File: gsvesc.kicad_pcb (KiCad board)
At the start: 4 copper layers, 111 x 111 mm, 147 parts, among them J1 Conn_01x06, J10 PHASE_C, J11 PHASE_B, J12 NTC, J13 Conn_01x02, J14 Conn_01x03, J2 Conn_01x06, J3 Conn_01x06, J4 Conn_01x05, J5 Conn_01x03, J6 USB_B_Mini, J7 BAT+, J8 BAT-, J9 PHASE_A, Q1 TPH2R608NH,L1Q, Q2 TPH2R608NH,L1Q, Q3 TPH2R608NH,L1Q, Q4 TPH2R608NH,L1Q, Q5 TPH2R608NH,L1Q, Q6 TPH2R608NH,L1Q, U1 STM32F405RGTx, U10 LM5008MM, U11 SN74LVC1G66DBVR, U12 LM5107, U13 SN74LVC1G66DBVR, U14 TPS5430DDA, U15 LM5107, U16 EYSGJNZWY, U17 TMP100NA_250, U2 SN74LVC1G66DBVR, U3 LM5107, U4 INA240A2, U5 INA240A2, U6 INA240A2, U7 SN74LVC1G66DBVR, U8 SN74LVC1G66DBVR, U9 SN74LVC1G66DBVR, Y1 X50328MSB2GI

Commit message: Ready for JLC
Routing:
- net /MCU/CURRENT_2: track 52.3 -> 48.8 mm
- net /Driver/SENS_FILTER: track 35.4 -> 36.2 mm
- net /MCU/I2C1_SCL: track 70.7 -> 70.1 mm

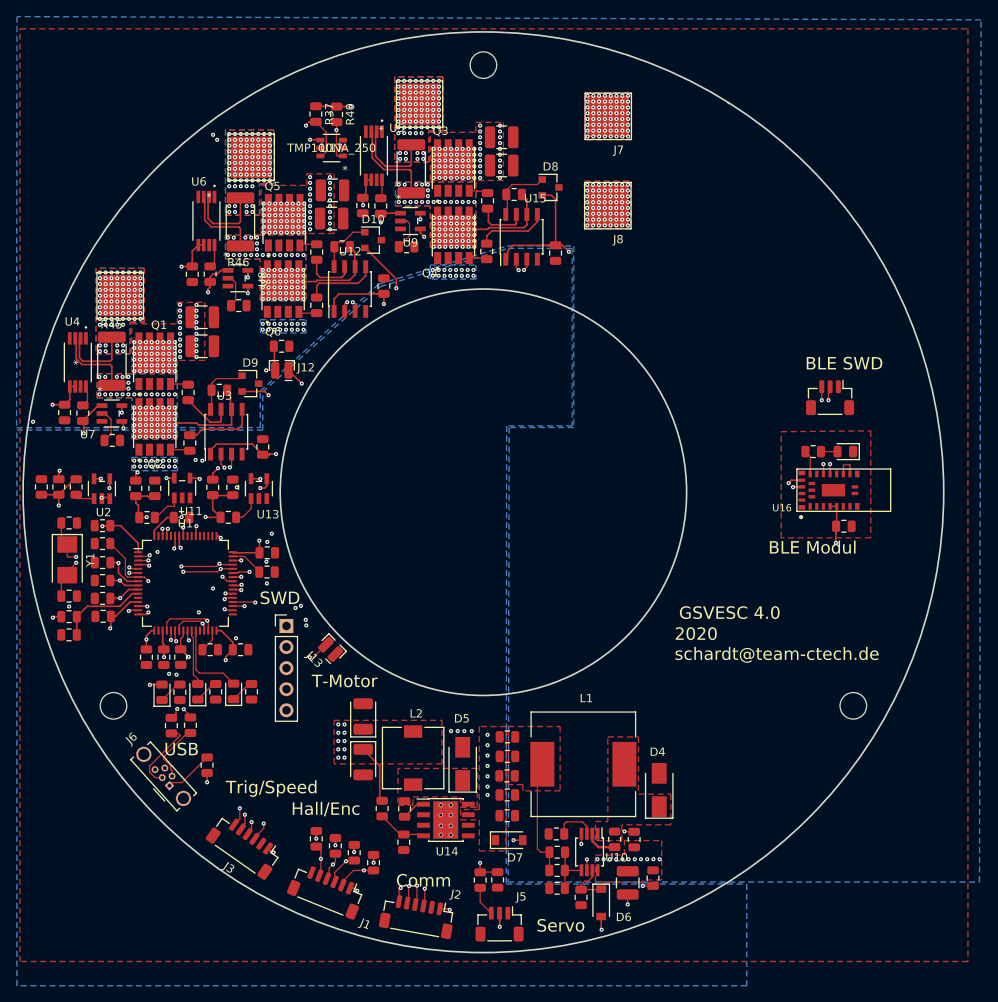
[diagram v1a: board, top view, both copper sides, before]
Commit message: some bug fixes for next pcb-run
- Add JST connector for Motor Temp
- Remove USB 5V
- add correct footprint for D8,9,10
- add JST connector for external off
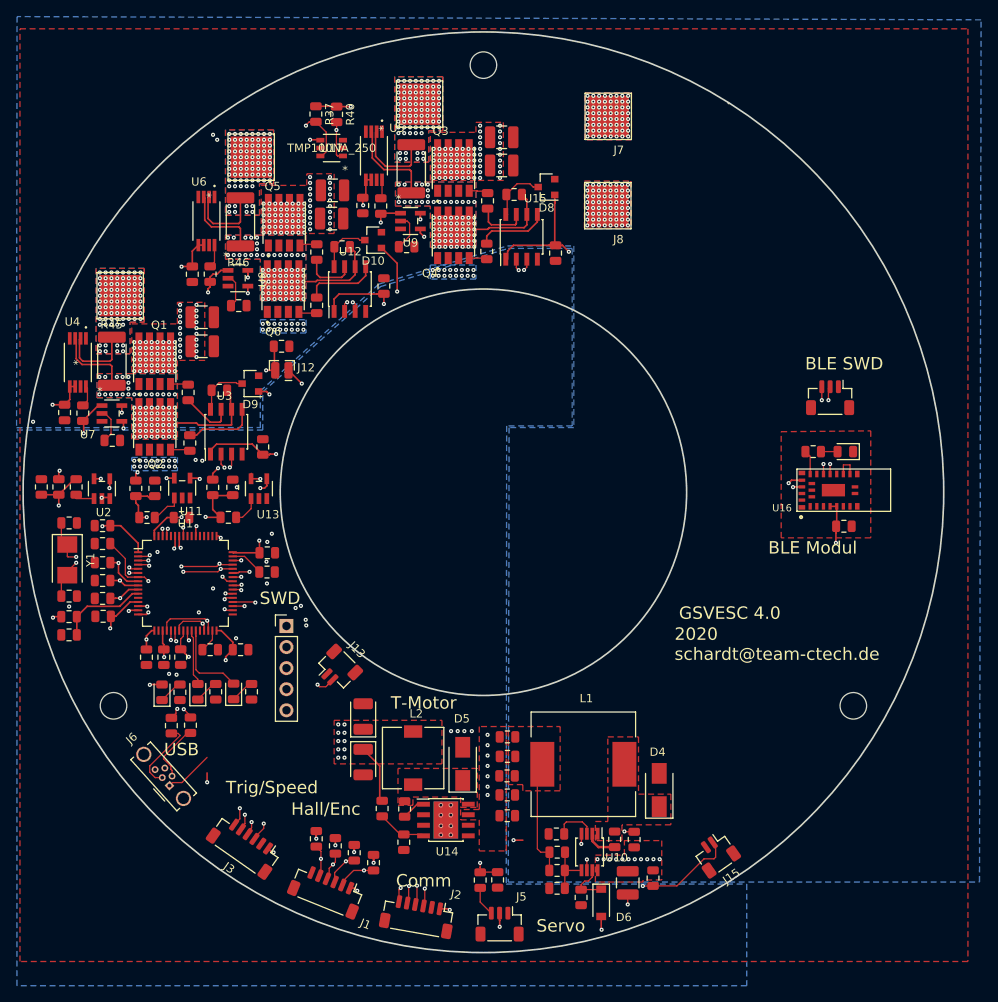
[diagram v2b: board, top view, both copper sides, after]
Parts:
- removed D7: B5819W, Diode_SMD:D_SOD-123
- removed R1: 0R00, Resistor_SMD:R_0805_2012Metric
- added J15: EXT off, Connector_JST:JST_SH_BM02B-SRSS-TB_1x02-1MP_P1.00mm_Vertical, F.Cu at (128.0, 143.6)
- J13: value Conn_01x02 -> T-Motor; footprint gsvesc:2pad_smd_testpin -> Connector_JST:JST_SH_BM02B-SRSS-TB_1x02-1MP_P1.00mm_Vertical
- R37, R40: value R -> 10k0
- moved J13 2.27 mm to (82.4, 121.3), turned to 315 degrees
- moved D8 0.50 mm to (107.6, 63.2), turned to 180 degrees
- turned D10 to 180 degrees
- turned D9 to 180 degrees
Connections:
- D10 pad 1: Net-(C27-Pad1) -> +12V
- D10 pad 2: +12V -> (no net)
- D10 pad 3: (no net) -> Net-(C27-Pad1)
- D8 pad 1: Net-(C32-Pad1) -> +12V
- D8 pad 2: +12V -> (no net)
- D8 pad 3: (no net) -> Net-(C32-Pad1)
- D9 pad 1: Net-(C21-Pad1) -> +12V
- D9 pad 2: +12V -> (no net)
- D9 pad 3: (no net) -> Net-(C21-Pad1)
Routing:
- net /Driver/EXT_OFF: track 10.6 -> 21.5 mm
- net +12V: track 46.9 -> 43.5 mm
- net /MCU/TEMP_MOTOR: track 54.3 -> 52.4 mm
- net Net-(C21-Pad1): track 7.24 -> 6.46 mm

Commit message: BUG Fixes, see BUGS.txt
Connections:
- net Net-(U1-Pad53) renamed /MCU/PC12
- U1 pad 51: Net-(U1-Pad51) -> /NRF/NRF_TX
- U1 pad 52: Net-(U1-Pad52) -> /NRF/NRF_RX
- U1 pad 57: /MCU/SERVO -> /MCU/PB5
- U1 pad 58: /NRF/NRF_TX -> /MCU/PB6
- U1 pad 59: /NRF/NRF_RX -> /MCU/SERVO
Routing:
- net +5V: track 42.1 -> 0.00 mm, vias 2 -> 0
- net Net-(J6-Pad1): track 5.94 -> 0.00 mm
- net /NRF/NRF_TX: track 111.3 -> 108.5 mm
- net /NRF/NRF_RX: track 111.6 -> 109.3 mm
- net /MCU/SERVO: track 65.4 -> 66.2 mm

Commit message: bug fixing
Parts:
- added U18: AQY282S, Package_SO:SO-4_4.4x4.3mm_P2.54mm, F.Cu at (126.2, 143.0)
- J15: value EXT off -> EXT_OFF; footprint Connector_JST:JST_SH_BM02B-SRSS-TB_1x02-1MP_P1.00mm_Vertical -> Connector_JST:JST_SH_BM06B-SRSS-TB_1x06-1MP_P1.00mm_Vertical
- moved J15 10.4 mm to (136.0, 137.0), turned to 221 degrees
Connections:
- J15 pad 1: /Driver/EXT_OFF -> VBAT
- J15 pad 2: GND -> +12V
- R12 pad 1: /Driver/EXT_OFF -> /Driver/EXT_OFF_DIRECT
- U10 pad 6: /Driver/EXT_OFF -> /Driver/EXT_OFF_DIRECT
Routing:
- net /Driver/EXT_OFF_DIRECT: track 0.00 -> 31.2 mm, vias 0 -> 2
- net +12V: track 43.5 -> 61.9 mm, vias 13 -> 14
- net /Driver/EXT_OFF: track 21.5 -> 10.7 mm, vias 2 -> 0
- net VCC: track 78.9 -> 81.0 mm, vias 38 -> 39
- net VBAT: track 25.7 -> 27.6 mm, vias 281 -> 282
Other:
- board text added: "4: drive max 2mA 5: pull to GND"
- board text added: "EXT off"
- board text added: "GND"
- board text added: "Ph A"
- board text added: "Ph B"
- board text added: "Ph C"
- board text added: "VBAT"

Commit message: add PDF
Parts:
- moved C24 0.45 mm to (70.9, 77.4), turned to 180 degrees
- moved C46 0.35 mm to (85.8, 65.4)
- moved R33 0.29 mm to (87.9, 65.4)
- moved U18 0.20 mm to (126.2, 142.8)
- moved C44 0.10 mm to (81.7, 63.6)
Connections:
- net /Driver/EXT_OFF renamed /Driver/EN_3V3
- J15 pad 5: /Driver/EXT_OFF_DIRECT -> /Driver/EN_12V
- R12 pad 1: /Driver/EXT_OFF_DIRECT -> /Driver/EN_12V
- U10 pad 6: /Driver/EXT_OFF_DIRECT -> /Driver/EN_12V
- U18 pad 4: /Driver/EXT_OFF_DIRECT -> Net-(U14-Pad5)
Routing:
- net /Driver/EXT_OFF_DIRECT: track 31.2 -> 0.00 mm, vias 2 -> 0
- net /Driver/EN_12V: track 0.00 -> 30.6 mm, vias 0 -> 3
- net Net-(U14-Pad5): track 0.00 -> 27.5 mm, vias 0 -> 2
- net Net-(C24-Pad1): track 4.13 -> 4.91 mm
- net GND: vias 120 -> 173
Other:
- board text removed: "4: drive max 2mA 5: pull to GND"

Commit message: temp
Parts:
- added C50: 10u0/75V, Capacitor_SMD:C_1210_3225Metric, F.Cu at (76.6, 63.0)
- added C51: 10u0/75V, Capacitor_SMD:C_1210_3225Metric, F.Cu at (117.5, 63.1)
- added C52: 10u0/75V, Capacitor_SMD:C_1210_3225Metric, F.Cu at (97.0, 63.1)
- added C53: CP, Capacitor_SMD:CP_Elec_10x12.5, F.Cu at (142.6, 79.7)
- added C54: CP, Capacitor_SMD:CP_Elec_10x12.5, F.Cu at (131.0, 79.5)
- added C55: CP, Capacitor_SMD:CP_Elec_10x12.5, F.Cu at (135.7, 92.6)
- added C56: CP, Capacitor_SMD:CP_Elec_10x12.5, F.Cu at (147.3, 92.5)
- J14: footprint Connector_JST:JST_SH_BM03B-SRSS-TB_1x03-1MP_P1.00mm_Vertical -> Connector_PinHeader_2.54mm:PinHeader_1x03_P2.54mm_Vertical
- moved J7 59.7 mm to (146.1, 105.7)
- moved J8 45.3 mm to (135.7, 105.7), turned to 270 degrees
- moved C29 38.8 mm to (70.6, 78.7), turned to 90 degrees
- moved R40 37.2 mm to (96.7, 88.7), turned to 180 degrees
- moved R35 37.1 mm to (125.1, 129.2), turned to 180 degrees
- moved U5 37.1 mm to (70.9, 92.9), turned to 180 degrees
- moved D8 37.0 mm to (74.0, 78.8), turned to 90 degrees
- moved R28 36.9 mm to (76.5, 53.1), turned to 180 degrees
- moved R37 36.2 mm to (96.6, 86.5), turned to 180 degrees
- moved D11 36.2 mm to (125.0, 126.2)
- moved J10 34.9 mm to (125.7, 63.3)
- moved U15 34.4 mm to (73.4, 83.8), turned to 0 degrees
- moved C46 34.3 mm to (70.5, 96.1), turned to 0 degrees
- moved R31 33.8 mm to (124.1, 69.2), turned to 180 degrees
- moved J11 33.7 mm to (105.5, 63.4)
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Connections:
- U17 pad 3: Net-(U17-Pad3) -> GND
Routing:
- net /Driver/SH_C: track 64.9 -> 1.64 mm, vias 70 -> 20
- net /MCU/I2C1_SDA: track 69.3 -> 6.15 mm, vias 3 -> 1
- net /POWER/CURR_FILTER: track 71.5 -> 15.7 mm, vias 5 -> 1
- net /MCU/I2C1_SCL: track 70.1 -> 18.2 mm, vias 3 -> 1
- net /Driver/SH_B: track 51.4 -> 8.68 mm, vias 71 -> 21
- net +12V: track 61.9 -> 20.0 mm, vias 14 -> 9
- net /MCU/L3: track 66.7 -> 25.0 mm, vias 2 -> 1
- net /MCU/H3: track 62.4 -> 20.9 mm, vias 2 -> 1
- net /MCU/CURRENT_3: track 75.0 -> 38.0 mm, vias 3 -> 2
- net /Driver/SH_A: track 32.9 -> 1.97 mm, vias 70 -> 21
- net /MCU/CURRENT_2: track 48.8 -> 19.5 mm, vias 3 -> 2
- net VCC: track 81.0 -> 52.2 mm, vias 39 -> 29
- net /MCU/L2: track 44.8 -> 24.9 mm, vias 2 -> 1
- net /MCU/H2: track 40.8 -> 21.4 mm, vias 2 -> 1
- net /MCU/ADC_TEMP: track 53.0 -> 34.1 mm, vias 3 -> 2
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- added copper zone on In1.Cu, net VCC
- removed copper zone on B.Cu, net +12V
- removed copper zone on B.Cu, net /Driver/SH_A
- removed copper zone on In1.Cu, net /Driver/SH_A
- removed copper zone on In2.Cu, net /Driver/SH_A
- removed copper zone on B.Cu, net /Driver/SH_B
- removed copper zone on In1.Cu, net /Driver/SH_B
- removed copper zone on In2.Cu, net /Driver/SH_B
- removed copper zone on B.Cu, net /Driver/SH_C
- removed copper zone on In1.Cu, net /Driver/SH_C
- removed copper zone on In2.Cu, net /Driver/SH_C
- removed copper zone on B.Cu, net /POWER/PHASE_A
- removed copper zone on In1.Cu, net /POWER/PHASE_A
- removed copper zone on In2.Cu, net /POWER/PHASE_A
- removed copper zone on B.Cu, net /POWER/PHASE_B
- removed copper zone on In1.Cu, net /POWER/PHASE_B
- removed copper zone on In2.Cu, net /POWER/PHASE_B
- removed copper zone on B.Cu, net /POWER/PHASE_C
- removed copper zone on In1.Cu, net /POWER/PHASE_C
- removed copper zone on In2.Cu, net /POWER/PHASE_C
- removed copper zone on In1.Cu, net GND
- removed copper zone on In2.Cu, net GND
- removed copper zone on In1.Cu, net VBAT
- removed copper zone on In2.Cu, net VBAT
- removed copper zone on In2.Cu, net VCC
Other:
- board text removed: "Ph A"
- board text removed: "Ph B"

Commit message: temp
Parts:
- moved J7 1.08 mm to (146.7, 104.8)
- moved J8 1.08 mm to (136.3, 104.8)
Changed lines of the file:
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@@
   )
   (module gsvesc:TestPoint_Pad_5.0x5.0mm (layer F.Cu)
-    (at 146.0998 105.6998 180)
+    (at 146.6998 104.7998 180)
     (descr "SMD rectangular pad as test Point, square 4.0mm side length")
     (tags "test point SMD pad rectangle square")
@@
   )
   (module gsvesc:TestPoint_Pad_5.0x5.0mm (layer F.Cu)
-    (at 135.6998 105.6998 270)
+    (at 136.2998 104.7998 270)
     (descr "SMD rectangular pad as test Point, square 4.0mm side length")
     (tags "test point SMD pad rectangle square")
@@
   (via (at 53.9758 100.6618) (size 0.5) (drill 0.2) (layers F.Cu B.Cu) (net 2) (status 30))
   (segment (start 54.695801 100.628) (end 54.211801 100.628) (width 0.2) (layer F.Cu) (net 2) (status 30))
-  (via (at 133.6998 103.6998) (size 0.5) (drill 0.2) (layers F.Cu B.Cu) (net 2))
-  (via (at 134.6998 103.6998) (size 0.5) (drill 0.2) (layers F.Cu B.Cu) (net 2))
-  (via (at 135.6998 103.6998) (size 0.5) (drill 0.2) (layers F.Cu B.Cu) (net 2))
-  (via (at 136.6998 103.6998) (size 0.5) (drill 0.2) (layers F.Cu B.Cu) (net 2))
-  (via (at 137.6998 103.6998) (size 0.5) (drill 0.2) (layers F.Cu B.Cu) (net 2))
-  (via (at 133.6998 104.6998) (size 0.5) (drill 0.2) (layers F.Cu B.Cu) (net 2))
-  (via (at 134.6998 104.6998) (size 0.5) (drill 0.2) (layers F.Cu B.Cu) (net 2))
-  (via (at 135.6998 104.6998) (size 0.5) (drill 0.2) (layers F.Cu B.Cu) (net 2))
-  (via (at 136.6998 104.6998) (size 0.5) (drill 0.2) (layers F.Cu B.Cu) (net 2))
-  (via (at 137.6998 104.6998) (size 0.5) (drill 0.2) (layers F.Cu B.Cu) (net 2))
-  (via (at 133.6998 105.6998) (size 0.5) (drill 0.2) (layers F.Cu B.Cu) (net 2))
-  (via (at 134.6998 105.6998) (size 0.5) (drill 0.2) (layers F.Cu B.Cu) (net 2))
-  (via (at 135.6998 105.6998) (size 0.5) (drill 0.2) (layers F.Cu B.Cu) (net 2))
-  (via (at 136.6998 105.6998) (size 0.5) (drill 0.2) (layers F.Cu B.Cu) (net 2))
-  (via (at 137.6998 105.6998) (size 0.5) (drill 0.2) (layers F.Cu B.Cu) (net 2))
-  (via (at 133.6998 106.6998) (size 0.5) (drill 0.2) (layers F.Cu B.Cu) (net 2))
-  (via (at 134.6998 106.6998) (size 0.5) (drill 0.2) (layers F.Cu B.Cu) (net 2))
-  (via (at 135.6998 106.6998) (size 0.5) (drill 0.2) (layers F.Cu B.Cu) (net 2))
-  (via (at 136.6998 106.6998) (size 0.5) (drill 0.2) (layers F.Cu B.Cu) (net 2))
-  (via (at 137.6998 106.6998) (size 0.5) (drill 0.2) (layers F.Cu B.Cu) (net 2))
-  (via (at 133.6998 107.6998) (size 0.5) (drill 0.2) (layers F.Cu B.Cu) (net 2))
-  (via (at 134.6998 107.6998) (size 0.5) (drill 0.2) (layers F.Cu B.Cu) (net 2))
-  (via (at 135.6998 107.6998) (size 0.5) (drill 0.2) (layers F.Cu B.Cu) (net 2))
-  (via (at 136.6998 107.6998) (size 0.5) (drill 0.2) (layers F.Cu B.Cu) (net 2))
-  (via (at 137.6998 107.6998) (size 0.5) (drill 0.2) (layers F.Cu B.Cu) (net 2))
+  (via (at 134.2998 102.7998) (size 0.5) (drill 0.2) (layers F.Cu B.Cu) (net 2))
+  (via (at 135.2998 102.7998) (size 0.5) (drill 0.2) (layers F.Cu B.Cu) (net 2))
+  (via (at 136.2998 102.7998) (size 0.5) (drill 0.2) (layers F.Cu B.Cu) (net 2))
+  (via (at 137.2998 102.7998) (size 0.5) (drill 0.2) (layers F.Cu B.Cu) (net 2))
+  (via (at 138.2998 102.7998) (size 0.5) (drill 0.2) (layers F.Cu B.Cu) (net 2))
+  (via (at 134.2998 103.7998) (size 0.5) (drill 0.2) (layers F.Cu B.Cu) (net 2))
+  (via (at 135.2998 103.7998) (size 0.5) (drill 0.2) (layers F.Cu B.Cu) (net 2))
+  (via (at 136.2998 103.7998) (size 0.5) (drill 0.2) (layers F.Cu B.Cu) (net 2))
+  (via (at 137.2998 103.7998) (size 0.5) (drill 0.2) (layers F.Cu B.Cu) (net 2))
+  (via (at 138.2998 103.7998) (size 0.5) (drill 0.2) (layers F.Cu B.Cu) (net 2))
+  (via (at 134.2998 104.7998) (size 0.5) (drill 0.2) (layers F.Cu B.Cu) (net 2))
+  (via (at 135.2998 104.7998) (size 0.5) (drill 0.2) (layers F.Cu B.Cu) (net 2))
+  (via (at 136.2998 104.7998) (size 0.5) (drill 0.2) (layers F.Cu B.Cu) (net 2))
+  (via (at 137.2998 104.7998) (size 0.5) (drill 0.2) (layers F.Cu B.Cu) (net 2))
+  (via (at 138.2998 104.7998) (size 0.5) (drill 0.2) (layers F.Cu B.Cu) (net 2))
+  (via (at 134.2998 105.7998) (size 0.5) (drill 0.2) (layers F.Cu B.Cu) (net 2))
+  (via (at 135.2998 105.7998) (size 0.5) (drill 0.2) (layers F.Cu B.Cu) (net 2))
+  (via (at 136.2998 105.7998) (size 0.5) (drill 0.2) (layers F.Cu B.Cu) (net 2))
+  (via (at 137.2998 105.7998) (size 0.5) (drill 0.2) (layers F.Cu B.Cu) (net 2))
+  (via (at 138.2998 105.7998) (size 0.5) (drill 0.2) (layers F.Cu B.Cu) (net 2))
+  (via (at 134.2998 106.7998) (size 0.5) (drill 0.2) (layers F.Cu B.Cu) (net 2))
+  (via (at 135.2998 106.7998) (size 0.5) (drill 0.2) (layers F.Cu B.Cu) (net 2))
+  (via (at 136.2998 106.7998) (size 0.5) (drill 0.2) (layers F.Cu B.Cu) (net 2))
+  (via (at 137.2998 106.7998) (size 0.5) (drill 0.2) (layers F.Cu B.Cu) (net 2))
+  (via (at 138.2998 106.7998) (size 0.5) (drill 0.2) (layers F.Cu B.Cu) (net 2))
   (via (at 109.8998 67.0998) (size 0.5) (drill 0.2) (layers F.Cu B.Cu) (net 2))
   (via (at 109.8998 69.7998) (size 0.5) (drill 0.2) (layers F.Cu B.Cu) (net 2))
@@
   (via (at 127.5998 62.2998) (size 0.5) (drill 0.2) (layers F.Cu B.Cu) (net 67))
   (via (at 113.3998 55.6998) (size 0.5) (drill 0.2) (layers F.Cu B.Cu) (net 68))
-  (via (at 148.0998 104.6998) (size 0.5) (drill 0.2) (layers F.Cu B.Cu) (net 68))
-  (via (at 144.0998 105.6998) (size 0.5) (drill 0.2) (layers F.Cu B.Cu) (net 68))
-  (via (at 145.0998 105.6998) (size 0.5) (drill 0.2) (layers F.Cu B.Cu) (net 68))
-  (via (at 145.0998 106.6998) (size 0.5) (drill 0.2) (layers F.Cu B.Cu) (net 68))
-  (via (at 146.0998 106.6998) (size 0.5) (drill 0.2) (layers F.Cu B.Cu) (net 68))
-  (via (at 147.0998 106.6998) (size 0.5) (drill 0.2) (layers F.Cu B.Cu) (net 68))
-  (via (at 148.0998 106.6998) (size 0.5) (drill 0.2) (layers F.Cu B.Cu) (net 68))
-  (via (at 146.0998 103.6998) (size 0.5) (drill 0.2) (layers F.Cu B.Cu) (net 68))
-  (via (at 145.0998 104.6998) (size 0.5) (drill 0.2) (layers F.Cu B.Cu) (net 68))
-  (via (at 148.0998 107.6998) (size 0.5) (drill 0.2) (layers F.Cu B.Cu) (net 68))
-  (via (at 144.0998 107.6998) (size 0.5) (drill 0.2) (layers F.Cu B.Cu) (net 68))
-  (via (at 145.0998 107.6998) (size 0.5) (drill 0.2) (layers F.Cu B.Cu) (net 68))
-  (via (at 146.0998 107.6998) (size 0.5) (drill 0.2) (layers F.Cu B.Cu) (net 68))
-  (via (at 147.0998 107.6998) (size 0.5) (drill 0.2) (layers F.Cu B.Cu) (net 68))
-  (via (at 147.0998 104.6998) (size 0.5) (drill 0.2) (layers F.Cu B.Cu) (net 68))
-  (via (at 146.0998 105.6998) (size 0.5) (drill 0.2) (layers F.Cu B.Cu) (net 68))
-  (via (at 147.0998 105.6998) (size 0.5) (drill 0.2) (layers F.Cu B.Cu) (net 68))
-  (via (at 148.0998 105.6998) (size 0.5) (drill 0.2) (layers F.Cu B.Cu) (net 68))
-  (via (at 144.0998 106.6998) (size 0.5) (drill 0.2) (layers F.Cu B.Cu) (net 68))
-  (via (at 148.0998 103.6998) (size 0.5) (drill 0.2) (layers F.Cu B.Cu) (net 68))
-  (via (at 144.0998 104.6998) (size 0.5) (drill 0.2) (layers F.Cu B.Cu) (net 68))
-  (via (at 144.0998 103.6998) (size 0.5) (drill 0.2) (layers F.Cu B.Cu) (net 68))
-  (via (at 147.0998 103.6998) (size 0.5) (drill 0.2) (layers F.Cu B.Cu) (net 68))
-  (via (at 146.0998 104.6998) (size 0.5) (drill 0.2) (layers F.Cu B.Cu) (net 68))
-  (via (at 145.0998 103.6998) (size 0.5) (drill 0.2) (layers F.Cu B.Cu) (net 68))
+  (via (at 148.6998 103.7998) (size 0.5) (drill 0.2) (layers F.Cu B.Cu) (net 68))
+  (via (at 144.6998 104.7998) (size 0.5) (drill 0.2) (layers F.Cu B.Cu) (net 68))
+  (via (at 145.6998 104.7998) (size 0.5) (drill 0.2) (layers F.Cu B.Cu) (net 68))
+  (via (at 145.6998 105.7998) (size 0.5) (drill 0.2) (layers F.Cu B.Cu) (net 68))
+  (via (at 146.6998 105.7998) (size 0.5) (drill 0.2) (layers F.Cu B.Cu) (net 68))
+  (via (at 147.6998 105.7998) (size 0.5) (drill 0.2) (layers F.Cu B.Cu) (net 68))
+  (via (at 148.6998 105.7998) (size 0.5) (drill 0.2) (layers F.Cu B.Cu) (net 68))
+  (via (at 146.6998 102.7998) (size 0.5) (drill 0.2) (layers F.Cu B.Cu) (net 68))
+  (via (at 145.6998 103.7998) (size 0.5) (drill 0.2) (layers F.Cu B.Cu) (net 68))
+  (via (at 148.6998 106.7998) (size 0.5) (drill 0.2) (layers F.Cu B.Cu) (net 68))
+  (via (at 144.6998 106.7998) (size 0.5) (drill 0.2) (layers F.Cu B.Cu) (net 68))
+  (via (at 145.6998 106.7998) (size 0.5) (drill 0.2) (layers F.Cu B.Cu) (net 68))
+  (via (at 146.6998 106.7998) (size 0.5) (drill 0.2) (layers F.Cu B.Cu) (net 68))
+  (via (at 147.6998 106.7998) (size 0.5) (drill 0.2) (layers F.Cu B.Cu) (net 68))
+  (via (at 147.6998 103.7998) (size 0.5) (drill 0.2) (layers F.Cu B.Cu) (net 68))
+  (via (at 146.6998 104.7998) (size 0.5) (drill 0.2) (layers F.Cu B.Cu) (net 68))
+  (via (at 147.6998 104.7998) (size 0.5) (drill 0.2) (layers F.Cu B.Cu) (net 68))
+  (via (at 148.6998 104.7998) (size 0.5) (drill 0.2) (layers F.Cu B.Cu) (net 68))
+  (via (at 144.6998 105.7998) (size 0.5) (drill 0.2) (layers F.Cu B.Cu) (net 68))
+  (via (at 148.6998 102.7998) (size 0.5) (drill 0.2) (layers F.Cu B.Cu) (net 68))
+  (via (at 144.6998 103.7998) (size 0.5) (drill 0.2) (layers F.Cu B.Cu) (net 68))
+  (via (at 144.6998 102.7998) (size 0.5) (drill 0.2) (layers F.Cu B.Cu) (net 68))
+  (via (at 147.6998 102.7998) (size 0.5) (drill 0.2) (layers F.Cu B.Cu) (net 68))
+  (via (at 146.6998 103.7998) (size 0.5) (drill 0.2) (layers F.Cu B.Cu) (net 68))
+  (via (at 145.6998 102.7998) (size 0.5) (drill 0.2) (layers F.Cu B.Cu) (net 68))
   (via (at 48.0998 115.1198) (size 0.5) (drill 0.2) (layers F.Cu B.Cu) (net 68))
   (segment (start 45.6998 91.4998) (end 45.6998 97.20787) (width 0.2) (layer In1.Cu) (net 68))
